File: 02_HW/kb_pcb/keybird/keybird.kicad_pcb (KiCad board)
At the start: 2 copper layers, 65 parts, among them J1 Adafruit_Feather_16_pin, J2 Adafruit_feather_12_pin, SW1 SW_Push, SW10 SW_Push, SW11 SW_Push, SW12 SW_Push, SW13 SW_Push, SW14 SW_Push, SW15 SW_Push, SW16 SW_Push, SW17 SW_Push, SW18 SW_Push, SW19 SW_Push, SW2 SW_Push, SW20 SW_Push, SW21 SW_Push, SW22 SW_Push, SW23 SW_Push, SW24 SW_Push, SW25 SW_Push, SW26 SW_Push, SW27 SW_Push, SW28 SW_Push, SW29 SW_Push, SW3 SW_Push, SW30 SW_Push, SW4 SW_Push, SW6 SW_Push, SW7 SW_Push, SW8 SW_Push, SW9 SW_Push

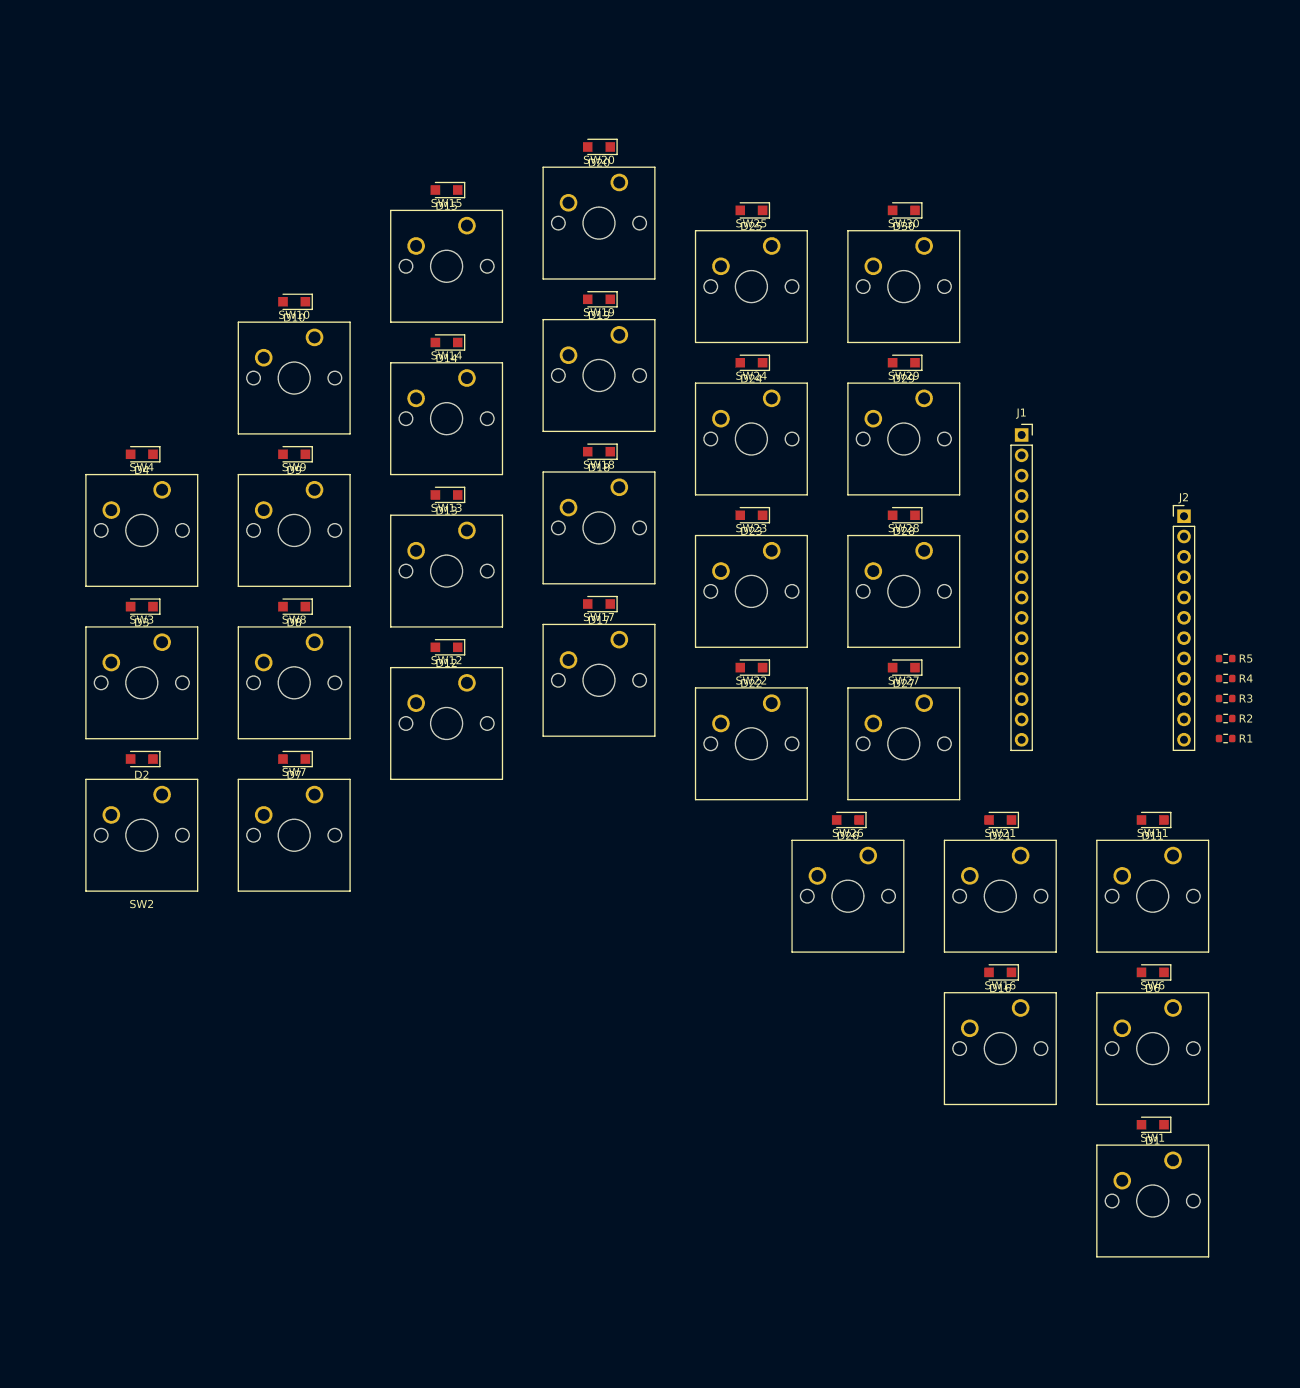
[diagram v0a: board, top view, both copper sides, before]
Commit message: Reverseddiodes for active low implementation
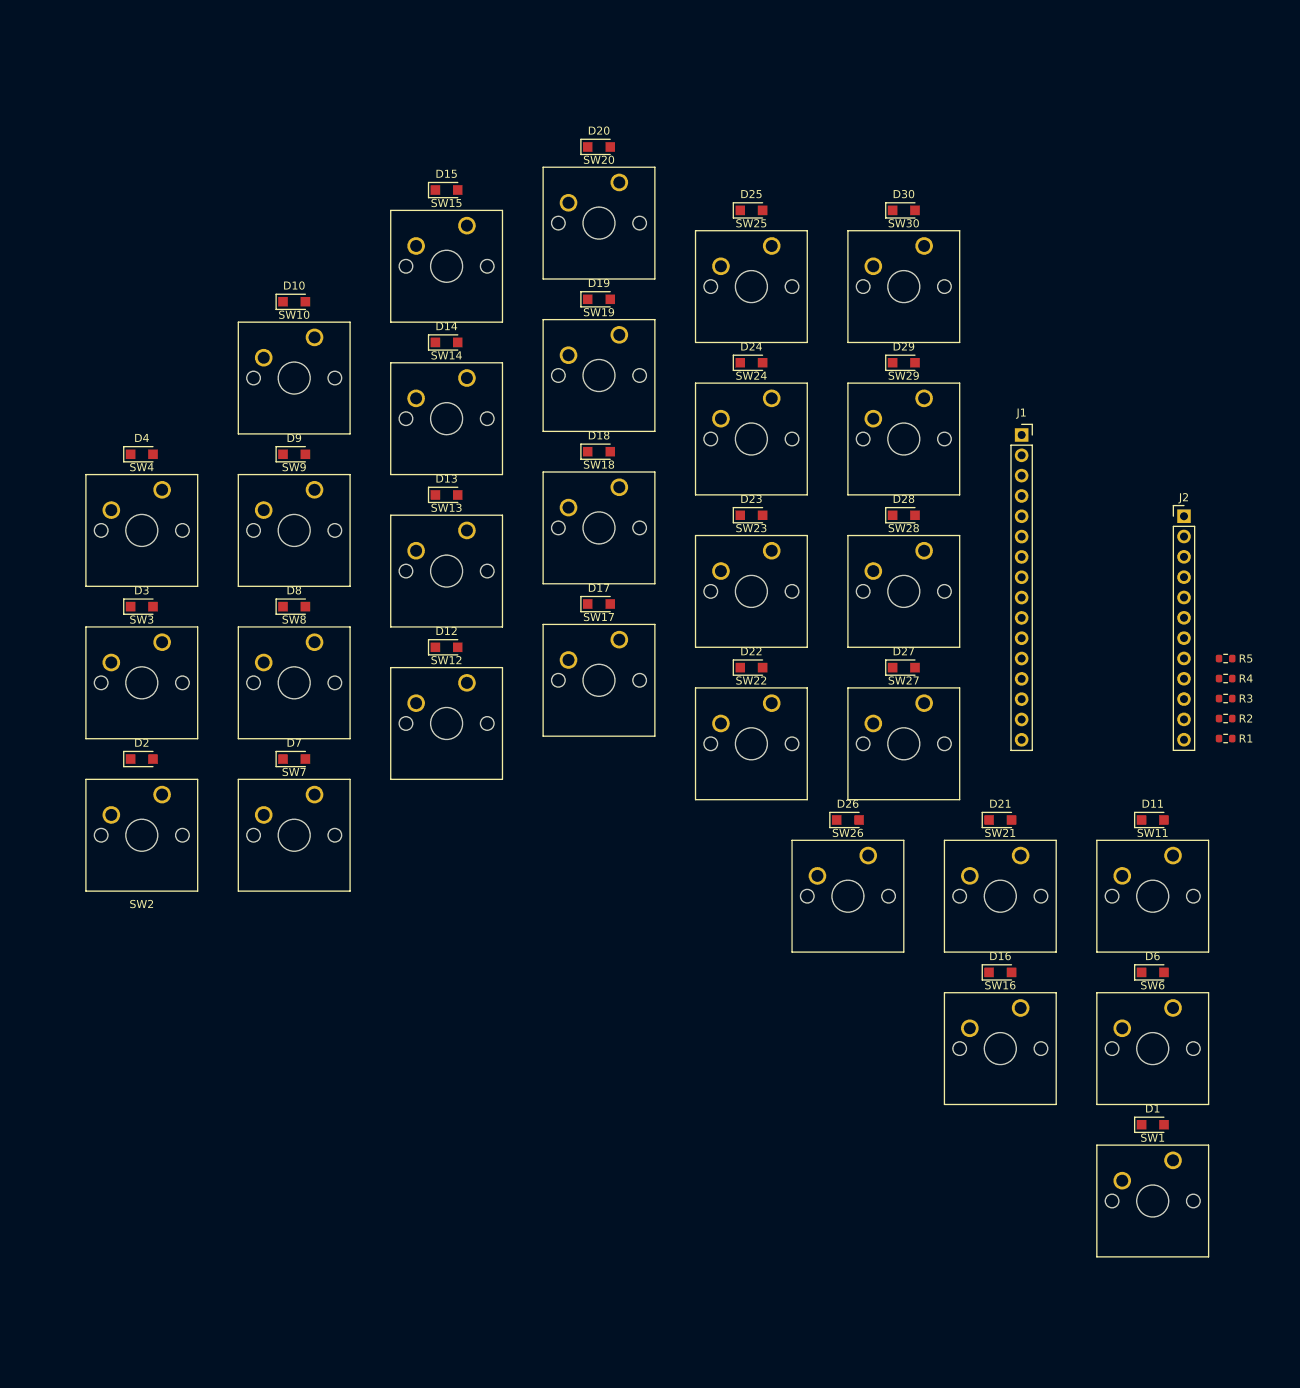
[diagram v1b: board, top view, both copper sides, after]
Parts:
- turned D1 to 0 degrees
- turned D10 to 0 degrees
- turned D11 to 0 degrees
- turned D12 to 0 degrees
- turned D13 to 0 degrees
- turned D14 to 0 degrees
- turned D15 to 0 degrees
- turned D16 to 0 degrees
- turned D17 to 0 degrees
- turned D18 to 0 degrees
- turned D19 to 0 degrees
- turned D2 to 0 degrees
- turned D20 to 0 degrees
- turned D21 to 0 degrees
- turned D22 to 0 degrees
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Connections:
- D1 pad 1: /Row_0 -> Net-(D1-K)
- D1 pad 2: Net-(D1-A) -> /Row_0
- D10 pad 1: /Row_4 -> Net-(D10-K)
- D10 pad 2: Net-(D10-A) -> /Row_4
- D11 pad 1: /Row_0 -> Net-(D11-K)
- D11 pad 2: Net-(D11-A) -> /Row_0
- D12 pad 1: /Row_1 -> Net-(D12-K)
- D12 pad 2: Net-(D12-A) -> /Row_1
- D13 pad 1: /Row_2 -> Net-(D13-K)
- D13 pad 2: Net-(D13-A) -> /Row_2
- D14 pad 1: /Row_3 -> Net-(D14-K)
- D14 pad 2: Net-(D14-A) -> /Row_3
- D15 pad 1: /Row_4 -> Net-(D15-K)
- D15 pad 2: Net-(D15-A) -> /Row_4
- D16 pad 1: /Row_0 -> Net-(D16-K)
- D16 pad 2: Net-(D16-A) -> /Row_0
- D17 pad 1: /Row_1 -> Net-(D17-K)
- D17 pad 2: Net-(D17-A) -> /Row_1
- D18 pad 1: /Row_2 -> Net-(D18-K)
- D18 pad 2: Net-(D18-A) -> /Row_2
- D19 pad 1: /Row_3 -> Net-(D19-K)
- D19 pad 2: Net-(D19-A) -> /Row_3
- D2 pad 1: /Row_1 -> Net-(D2-K)
- D2 pad 2: Net-(D2-A) -> /Row_1
- D20 pad 1: /Row_4 -> Net-(D20-K)
- D20 pad 2: Net-(D20-A) -> /Row_4
- D21 pad 1: /Row_0 -> Net-(D21-K)
- D21 pad 2: Net-(D21-A) -> /Row_0
- D22 pad 1: /Row_1 -> Net-(D22-K)
- D22 pad 2: Net-(D22-A) -> /Row_1
- D23 pad 1: /Row_2 -> Net-(D23-K)
- D23 pad 2: Net-(D23-A) -> /Row_2
- D24 pad 1: /Row_3 -> Net-(D24-K)
- D24 pad 2: Net-(D24-A) -> /Row_3
- D25 pad 1: /Row_4 -> Net-(D25-K)
- D25 pad 2: Net-(D25-A) -> /Row_4
- D26 pad 1: /Row_0 -> Net-(D26-K)
- D26 pad 2: Net-(D26-A) -> /Row_0
- D27 pad 1: /Row_1 -> Net-(D27-K)
- D27 pad 2: Net-(D27-A) -> /Row_1
- D28 pad 1: /Row_2 -> Net-(D28-K)
- D28 pad 2: Net-(D28-A) -> /Row_2
- D29 pad 1: /Row_3 -> Net-(D29-K)
- D29 pad 2: Net-(D29-A) -> /Row_3
- D3 pad 1: /Row_2 -> Net-(D3-K)
- D3 pad 2: Net-(D3-A) -> /Row_2
- D30 pad 1: /Row_4 -> Net-(D30-K)
- D30 pad 2: Net-(D30-A) -> /Row_4
- D4 pad 1: /Row_3 -> Net-(D4-K)
- D4 pad 2: Net-(D4-A) -> /Row_3
- D6 pad 1: /Row_0 -> Net-(D6-K)
- D6 pad 2: Net-(D6-A) -> /Row_0
- D7 pad 1: /Row_1 -> Net-(D7-K)
- D7 pad 2: Net-(D7-A) -> /Row_1
- D8 pad 1: /Row_2 -> Net-(D8-K)
- D8 pad 2: Net-(D8-A) -> /Row_2
- D9 pad 1: /Row_3 -> Net-(D9-K)
- D9 pad 2: Net-(D9-A) -> /Row_3
- SW1 pad 2: Net-(D1-A) -> Net-(D1-K)
- SW10 pad 2: Net-(D10-A) -> Net-(D10-K)
- SW11 pad 2: Net-(D11-A) -> Net-(D11-K)
- SW12 pad 2: Net-(D12-A) -> Net-(D12-K)
- SW13 pad 2: Net-(D13-A) -> Net-(D13-K)
- SW14 pad 2: Net-(D14-A) -> Net-(D14-K)
- SW15 pad 2: Net-(D15-A) -> Net-(D15-K)
- SW16 pad 2: Net-(D16-A) -> Net-(D16-K)
- SW17 pad 2: Net-(D17-A) -> Net-(D17-K)
- SW18 pad 2: Net-(D18-A) -> Net-(D18-K)
- SW19 pad 2: Net-(D19-A) -> Net-(D19-K)
- SW2 pad 2: Net-(D2-A) -> Net-(D2-K)
- SW20 pad 2: Net-(D20-A) -> Net-(D20-K)
- SW21 pad 2: Net-(D21-A) -> Net-(D21-K)
- SW22 pad 2: Net-(D22-A) -> Net-(D22-K)
- SW23 pad 2: Net-(D23-A) -> Net-(D23-K)
- SW24 pad 2: Net-(D24-A) -> Net-(D24-K)
- SW25 pad 2: Net-(D25-A) -> Net-(D25-K)
- SW26 pad 2: Net-(D26-A) -> Net-(D26-K)
- SW27 pad 2: Net-(D27-A) -> Net-(D27-K)
- SW28 pad 2: Net-(D28-A) -> Net-(D28-K)
- SW29 pad 2: Net-(D29-A) -> Net-(D29-K)
- SW3 pad 2: Net-(D3-A) -> Net-(D3-K)
- SW30 pad 2: Net-(D30-A) -> Net-(D30-K)
- SW4 pad 2: Net-(D4-A) -> Net-(D4-K)
- SW6 pad 2: Net-(D6-A) -> Net-(D6-K)
- SW7 pad 2: Net-(D7-A) -> Net-(D7-K)
- SW8 pad 2: Net-(D8-A) -> Net-(D8-K)
- SW9 pad 2: Net-(D9-A) -> Net-(D9-K)

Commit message: Updated uart connector to match ftdi cable pinout
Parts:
- added D31: LED, LED_SMD:LED_0603_1608Metric, F.Cu at (139.5, 53.0)
- added D32: LED, LED_SMD:LED_0603_1608Metric, F.Cu at (139.5, 44.1)
- added D5: LED, LED_SMD:LED_0603_1608Metric, F.Cu at (139.5, 62.0)
- added J4: FTDI UART, Connector_PinHeader_2.54mm:PinHeader_1x06_P2.54mm_Vertical, F.Cu at (149.4, 44.0)
- added R6: R_US, Resistor_SMD:R_0603_1608Metric, F.Cu at (139.5, 66.5)
- added R7: R_US, Resistor_SMD:R_0603_1608Metric, F.Cu at (139.5, 57.5)
- added R8: R_US, Resistor_SMD:R_0603_1608Metric, F.Cu at (139.5, 48.6)
- added SW5: Power enable, Button_Switch_THT:SW_Slide-03_Wuerth-WS-SLTV_10x2.5x6.4_P2.54mm, F.Cu at (157.0, 60.0)
- moved R1 19.8 mm to (146.2, 113.0)
- moved R2 19.8 mm to (146.2, 110.5)
- moved R3 19.8 mm to (146.2, 108.0)
- moved R4 19.8 mm to (146.2, 105.5)
- moved R5 19.8 mm to (146.2, 103.0)
- moved J1 3.54 mm to (140.7, 75.4)
- moved J2 3.54 mm to (161.0, 85.5)
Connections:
- J1 pad 10: /Col_4 -> unconnected-(J1-Pin_10-Pad10)
- J1 pad 11: /Col_5 -> unconnected-(J1-Pin_11-Pad11)
- J1 pad 12: unconnected-(J1-Pin_12-Pad12) -> /Row_4
- J1 pad 13: unconnected-(J1-Pin_13-Pad13) -> /Row_3
- J1 pad 14: unconnected-(J1-Pin_14-Pad14) -> /Row_2
- J1 pad 15: unconnected-(J1-Pin_15-Pad15) -> /Row_1
- J1 pad 16: unconnected-(J1-Pin_16-Pad16) -> /Row_0
- J1 pad 2: unconnected-(J1-Pin_2-Pad2) -> +3.3V
- J1 pad 4: unconnected-(J1-Pin_4-Pad4) -> GNDREF
- J1 pad 5: unconnected-(J1-Pin_5-Pad5) -> /RED_LED
- J1 pad 6: /Col_0 -> /BLUE_LED
- J1 pad 7: /Col_1 -> /GREEN_LED
- J1 pad 8: /Col_2 -> unconnected-(J1-Pin_8-Pad8)
- J1 pad 9: /Col_3 -> unconnected-(J1-Pin_9-Pad9)
- J2 pad 10: /Row_2 -> /Col_2
- J2 pad 11: /Row_1 -> /Col_1
- J2 pad 12: /Row_0 -> /Col_0
- J2 pad 2: unconnected-(J2-Pin_2-Pad2) -> /EN
- J2 pad 4: unconnected-(J2-Pin_4-Pad4) -> /UART_TX
- J2 pad 5: unconnected-(J2-Pin_5-Pad5) -> /UART_RX
- J2 pad 7: unconnected-(J2-Pin_7-Pad7) -> /Col_5
- J2 pad 8: /Row_4 -> /Col_4
- J2 pad 9: /Row_3 -> /Col_3

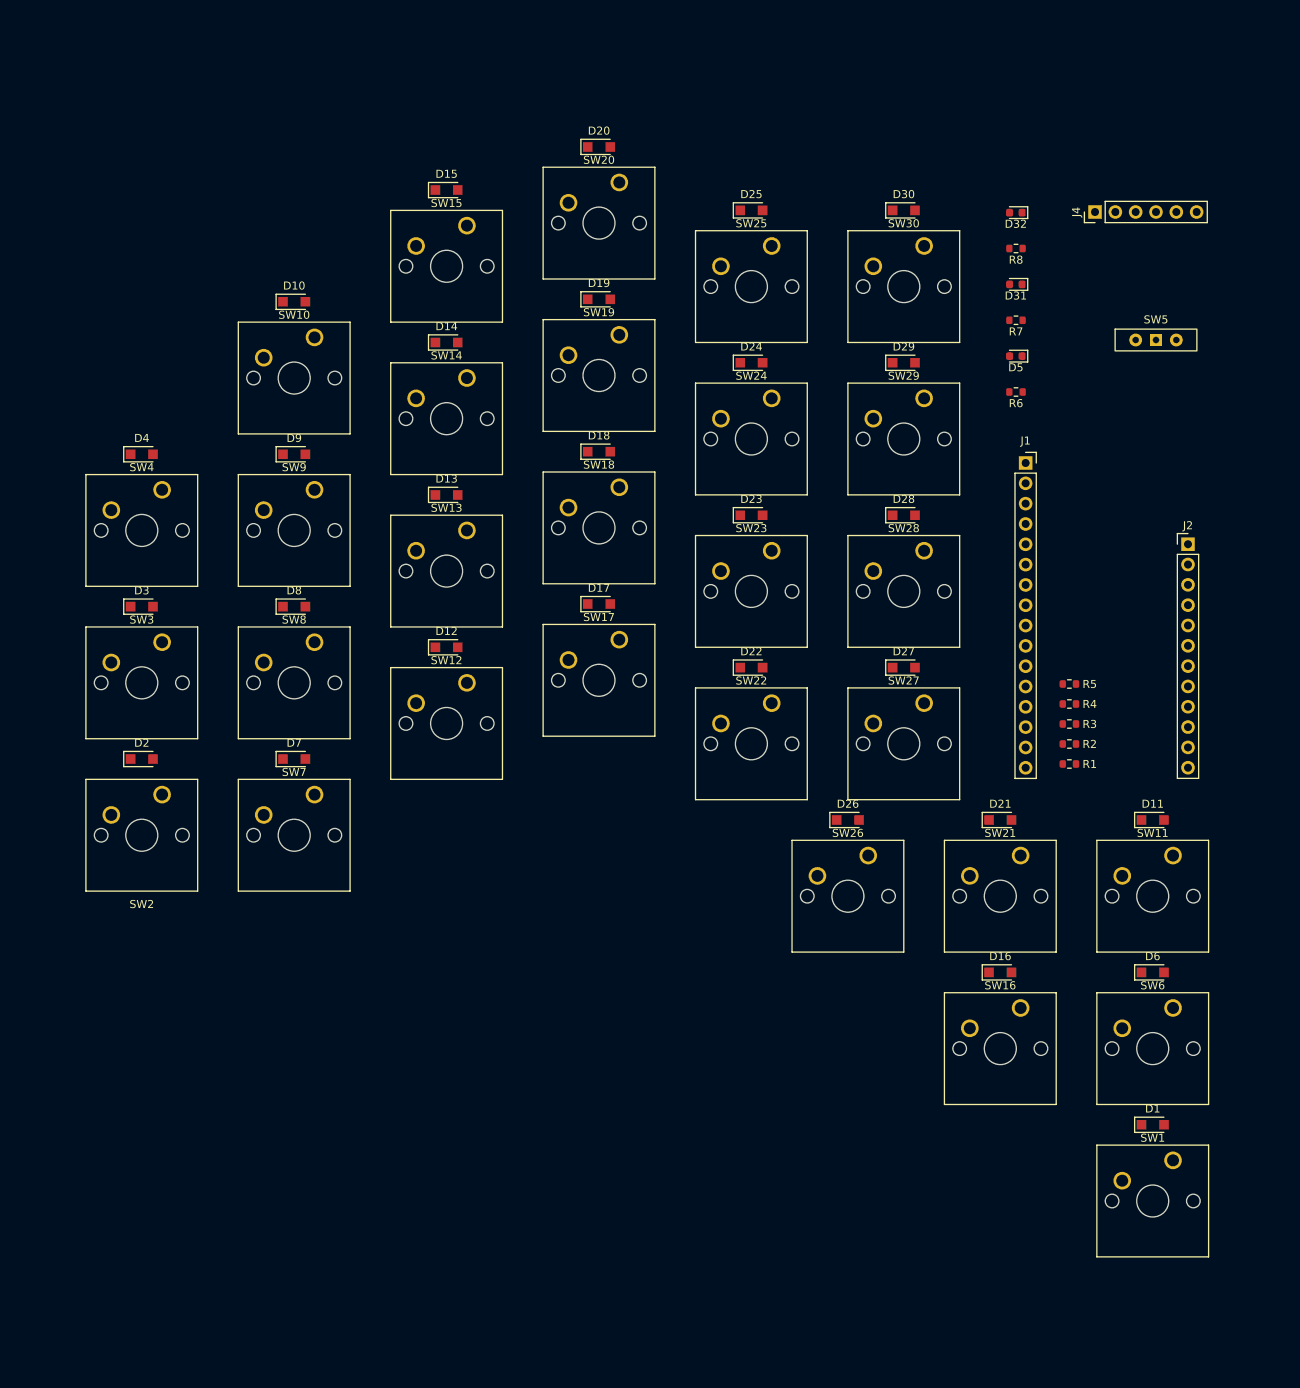
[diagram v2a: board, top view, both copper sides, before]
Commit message: Added board outline
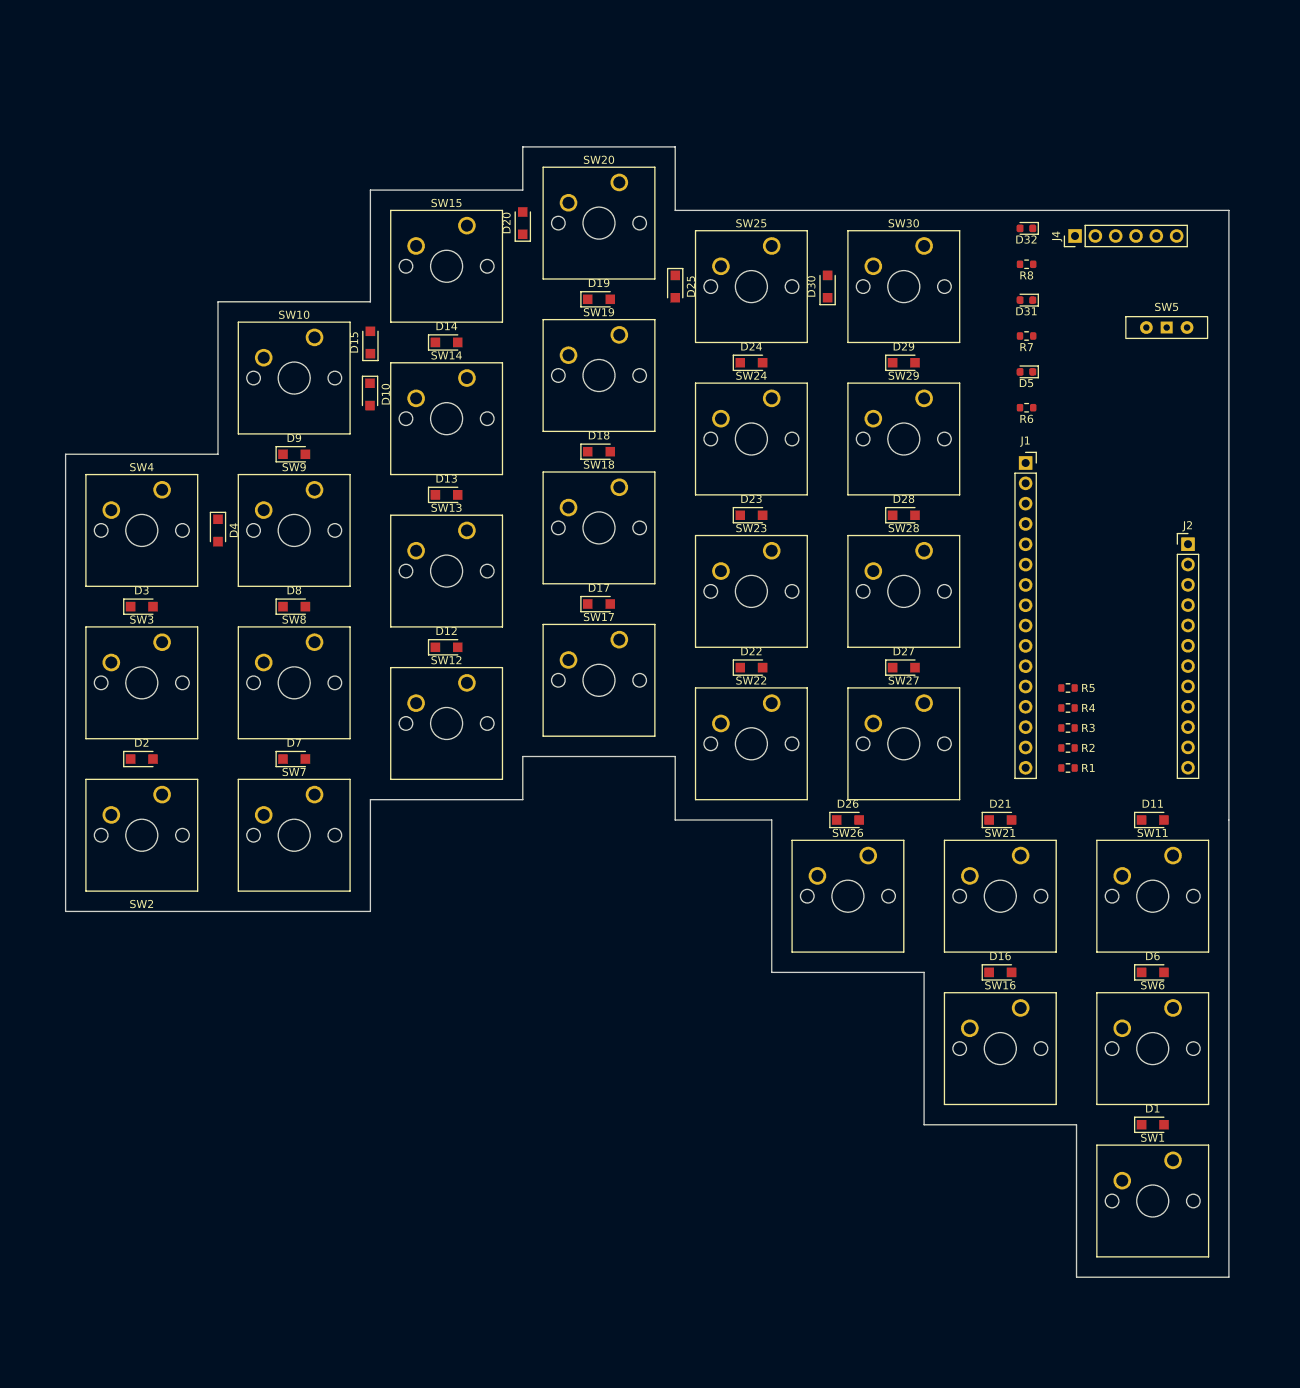
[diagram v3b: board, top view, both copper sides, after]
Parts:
- moved D15 21.3 mm to (58.8, 60.3), turned to 90 degrees
- moved D10 15.0 mm to (58.8, 66.8), turned to -90 degrees
- moved D20 13.5 mm to (77.8, 45.4), turned to 90 degrees
- moved D4 13.5 mm to (39.8, 83.8), turned to -90 degrees
- moved D25 13.5 mm to (96.9, 53.3), turned to -90 degrees
- moved D30 13.5 mm to (116.0, 53.3), turned to 90 degrees
- moved J4 3.91 mm to (146.9, 47.0)
- moved D32 2.37 mm to (140.8, 46.0)
- moved D5 2.37 mm to (140.8, 64.0)
- moved D31 2.37 mm to (140.8, 55.0)
- moved R6 2.37 mm to (140.8, 68.5)
- moved R7 2.37 mm to (140.8, 59.5)
- moved R8 2.37 mm to (140.8, 50.5)
- moved SW5 2.05 mm to (158.3, 58.4)
- moved R1 0.53 mm to (146.0, 113.5)
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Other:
- board outline added: 145.4 x 141.3 mm
